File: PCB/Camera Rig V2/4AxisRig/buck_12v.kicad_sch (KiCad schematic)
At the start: 9 parts, among them U2 AN_SY8105

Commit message: PCB V2 first draft
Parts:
- C14, C15, C16: footprint (none) -> Capacitor_SMD:C_0603_1608Metric_Pad1.08x0.95mm_HandSolder
- C17, C18: footprint (none) -> Capacitor_SMD:C_1206_3216Metric_Pad1.33x1.80mm_HandSolder
- L1: footprint footprints:DR74 -> DR74-4R7-R:DR74; Unique FP y -> (none)
- U2: Unique FP y -> (none)
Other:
- moved on the sheet: C15
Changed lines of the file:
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@@
 	(wire
 		(pts
-			(xy 134.62 74.93) (xy 137.16 74.93)
+			(xy 133.35 74.93) (xy 137.16 74.93)
 		)
 		(stroke
@@
 	(wire
 		(pts
-			(xy 127 74.93) (xy 123.19 74.93)
+			(xy 125.73 74.93) (xy 123.19 74.93)
 		)
 		(stroke
@@
 			)
 		)
-		(property "Unique FP" ""
-			(at 147.32 105.41 0)
-			(effects
-				(font
-					(size 1.27 1.27)
-				)
-			)
-		)
 		(pin "2"
 		)
@@
 			)
 		)
-		(property "Footprint" ""
+		(property "Footprint" "Capacitor_SMD:C_0603_1608Metric_Pad1.08x0.95mm_HandSolder"
 			(at 94.9452 97.79 0)
 			(effects
@@
 		)
 		(property "Part Number" ""
-			(at 93.98 93.98 0)
-			(effects
-				(font
-					(size 1.27 1.27)
-				)
-			)
-		)
-		(property "Unique FP" ""
 			(at 93.98 93.98 0)
 			(effects
@@
 		(fields_autoplaced yes)
 		(property "Reference" "U2"
-			(at 125.3333 81.28 0)
+			(at 125.3333 80.01 0)
 			(effects
 				(font
@@
 		)
 		(property "Value" "AN_SY8105"
-			(at 125.3333 83.82 0)
+			(at 125.3333 82.55 0)
 			(effects
 				(font
@@
 					(size 1.27 1.27)
 				)
-			)
-		)
-		(property "Unique FP" "y"
-			(at 123.19 92.71 0)
-			(effects
-				(font
-					(size 1.27 1.27)
-				)
+				(hide yes)
 			)
 		)
@@
 			)
 		)
-		(property "Footprint" ""
+		(property "Footprint" "Capacitor_SMD:C_1206_3216Metric_Pad1.33x1.80mm_HandSolder"
 			(at 190.1952 99.06 0)
 			(effects
@@
 			)
 		)
-		(property "Datasheet" "~"
+		(property "Datasheet" "https://mm.digikey.com/Volume0/opasdata/d220001/medias/docus/506/TMK316BBJ226ML-T_SS.pdf"
 			(at 189.23 95.25 0)
 			(effects
@@
 		)
 		(property "Part Number" ""
-			(at 189.23 95.25 0)
-			(effects
-				(font
-					(size 1.27 1.27)
-				)
-			)
-		)
-		(property "Unique FP" ""
 			(at 189.23 95.25 0)
 			(effects
@@
 	(symbol
 		(lib_id "Device:C")
-		(at 130.81 74.93 270)
+		(at 129.54 74.93 270)
 		(unit 1)
 		(exclude_from_sim no)
@@
 		(fields_autoplaced yes)
 		(property "Reference" "C15"
-			(at 130.81 67.31 90)
+			(at 129.54 67.31 90)
 			(effects
 				(font
@@
 		)
 		(property "Value" "100nF"
-			(at 130.81 69.85 90)
-			(effects
-				(font
-					(size 1.27 1.27)
-				)
-			)
-		)
-		(property "Footprint" ""
-			(at 127 75.8952 0)
+			(at 129.54 69.85 90)
+			(effects
+				(font
+					(size 1.27 1.27)
+				)
+			)
+		)
+		(property "Footprint" "Capacitor_SMD:C_0603_1608Metric_Pad1.08x0.95mm_HandSolder"
+			(at 125.73 75.8952 0)
 			(effects
 				(font
@@
 		)
 		(property "Datasheet" "~"
-			(at 130.81 74.93 0)
+			(at 129.54 74.93 0)
 			(effects
 				(font
@@
 		)
 		(property "Description" "Unpolarized capacitor"
-			(at 130.81 74.93 0)
+			(at 129.54 74.93 0)
 			(effects
 				(font
@@
 		)
 		(property "Link" ""
-			(at 130.81 74.93 0)
+			(at 129.54 74.93 0)
 			(effects
 				(font
@@
 		)
 		(property "Part Number" ""
-			(at 130.81 74.93 0)
-			(effects
-				(font
-					(size 1.27 1.27)
-				)
-			)
-		)
-		(property "Unique FP" ""
-			(at 130.81 74.93 0)
+			(at 129.54 74.93 0)
 			(effects
 				(font
@@
 			)
 		)
-		(property "Footprint" "footprints:DR74"
+		(property "Footprint" "DR74-4R7-R:DR74"
 			(at 142.24 90.17 0)
 			(effects
@@
 					(size 1.27 1.27)
 				)
-			)
-		)
-		(property "Unique FP" "y"
-			(at 142.24 90.17 0)
-			(effects
-				(font
-					(size 1.27 1.27)
-				)
+				(hide yes)
 			)
 		)
@@
 			)
 		)
-		(property "Footprint" ""
+		(property "Footprint" "Capacitor_SMD:C_1206_3216Metric_Pad1.33x1.80mm_HandSolder"
 			(at 178.7652 99.06 0)
 			(effects
@@
 			)
 		)
-		(property "Datasheet" "~"
+		(property "Datasheet" "https://mm.digikey.com/Volume0/opasdata/d220001/medias/docus/506/TMK316BBJ226ML-T_SS.pdf"
 			(at 177.8 95.25 0)
 			(effects
@@
 		)
 		(property "Part Number" ""
-			(at 177.8 95.25 0)
-			(effects
-				(font
-					(size 1.27 1.27)
-				)
-			)
-		)
-		(property "Unique FP" ""
 			(at 177.8 95.25 0)
 			(effects
@@
 		(dnp no)
 		(property "Reference" "R15"
-			(at 142.748 97.282 90)
+			(at 149.606 94.234 0)
 			(effects
 				(font
@@
 		)
 		(property "Value" "200k"
-			(at 145.034 97.282 90)
+			(at 149.606 96.774 0)
 			(effects
 				(font
@@
 		)
 		(property "Part Number" ""
-			(at 147.32 95.25 0)
-			(effects
-				(font
-					(size 1.27 1.27)
-				)
-			)
-		)
-		(property "Unique FP" ""
 			(at 147.32 95.25 0)
 			(effects
@@
 			)
 		)
-		(property "Footprint" ""
+		(property "Footprint" "Capacitor_SMD:C_0603_1608Metric_Pad1.08x0.95mm_HandSolder"
 			(at 160.9852 99.06 0)
 			(effects
@@
 			(at 160.02 95.25 0)
 			(effects
-				(font
-					(size 1.27 1.27)
-				)
-			)
-		)
-		(property "Unique FP" ""
-			(at 160.02 95.25 0)
-			(effects

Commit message: Updated figs
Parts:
- added D6: SMAJ10CA-13-F, SMAJ10CA-13-F:SMA_DIO, symbol Device:D_Schottky
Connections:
- net GND: now also D6.1 (K)
- net VOUT_12V: now also D6.2 (A)
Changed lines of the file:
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@@
+	)
+	(junction
+		(at 203.2 90.17)
+		(diameter 0)
+		(color 0 0 0 0)
 	)
 	(junction
@@
 	(wire
 		(pts
+			(xy 203.2 91.44) (xy 203.2 90.17)
+		)
+		(stroke
+			(width 0)
+			(type default)
+		)
+	)
+	(wire
+		(pts
 			(xy 137.16 90.17) (xy 138.43 90.17)
 		)
@@
 	(wire
 		(pts
+			(xy 203.2 90.17) (xy 208.28 90.17)
+		)
+		(stroke
+			(width 0)
+			(type default)
+		)
+	)
+	(wire
+		(pts
 			(xy 147.32 100.33) (xy 147.32 99.06)
 		)
@@
 	(wire
 		(pts
-			(xy 189.23 90.17) (xy 194.31 90.17)
+			(xy 189.23 90.17) (xy 203.2 90.17)
 		)
 		(stroke
@@
 	(hierarchical_label "VOUT_12V"
 		(shape output)
-		(at 194.31 90.17 0)
+		(at 208.28 90.17 0)
 		(effects
 			(font
@@
 			)
 			(justify right)
+		)
+	)
+	(symbol
+		(lib_id "Device:D_Schottky")
+		(at 203.2 95.25 90)
+		(unit 1)
+		(exclude_from_sim no)
+		(in_bom yes)
+		(on_board yes)
+		(dnp no)
+		(fields_autoplaced yes)
+		(property "Reference" "D6"
+			(at 205.74 94.2974 90)
+			(effects
+				(font
+					(size 1.27 1.27)
+				)
+				(justify right)
+			)
+		)
+		(property "Value" "SMAJ10CA-13-F"
+			(at 205.74 96.8374 90)
+			(effects
+				(font
+					(size 1.27 1.27)
+				)
+				(justify right)
+			)
+		)
+		(property "Footprint" "SMAJ10CA-13-F:SMA_DIO"
+			(at 203.2 95.25 0)
+			(effects
+				(font
+					(size 1.27 1.27)
+				)
+				(hide yes)
+			)
+		)
+		(property "Datasheet" "https://www.diodes.com/assets/Datasheets/SMAJ5.0CA-SMAJ200CA.pdf"
+			(at 203.2 95.25 0)
+			(effects
+				(font
+					(size 1.27 1.27)
+				)
+				(hide yes)
+			)
+		)
+		(property "Description" "Schottky diode"
+			(at 203.2 95.25 0)
+			(effects
+				(font
+					(size 1.27 1.27)
+				)
+				(hide yes)
+			)
+		)
+		(property "Link" ""
+			(at 203.2 95.25 0)
+			(effects
+				(font
+					(size 1.27 1.27)
+				)
+			)
+		)
+		(property "Part Number" ""
+			(at 203.2 95.25 0)
+			(effects
+				(font
+					(size 1.27 1.27)
+				)
+			)
+		)
+		(pin "2"
+		)
+		(pin "1"
+		)
+		(instances
+			(project "4AxisRig"
+				(path "/afe116b2-64d1-4090-9b3d-2b16ecf9512b/ea896716-9127-4765-8811-1397e4644c8c"
+					(reference "D6")
+					(unit 1)
+				)
+			)
 		)
 	)
@@
 					(unit 1)
 				)
+			)
+		)
+	)
+	(symbol
+		(lib_id "power:GND")
+		(at 203.2 99.06 0)
+		(unit 1)
+		(exclude_from_sim no)
+		(in_bom yes)
+		(on_board yes)
+		(dnp no)
+		(fields_autoplaced yes)
+		(property "Reference" "#PWR0101"
+			(at 203.2 105.41 0)
+			(effects
+				(font
+					(size 1.27 1.27)
+				)
+				(hide yes)
+			)
+		)
+		(property "Value" "GND"
+			(at 203.2 104.14 0)
+			(effects
+				(font
+					(size 1.27 1.27)
+				)
+			)
+		)
+		(property "Footprint" ""
+			(at 203.2 99.06 0)
+			(effects
+				(font
+					(size 1.27 1.27)
+				)
+				(hide yes)
+			)
+		)
+		(property "Datasheet" ""
+			(at 203.2 99.06 0)
+			(effects
+				(font
+					(size 1.27 1.27)
+				)
+				(hide yes)
+			)
+		)
+		(property "Description" "Power symbol creates a global label with name \"GND\" , ground"
+			(at 203.2 99.06 0)
+			(effects
+				(font
+					(size 1.27 1.27)
+				)
+				(hide yes)
+			)
+		)
+		(pin "1"
+		)
+		(instances
+			(project "4AxisRig"
+				(path "/afe116b2-64d1-4090-9b3d-2b16ecf9512b/ea896716-9127-4765-8811-1397e4644c8c"
+					(reference "#PWR0101")
+					(unit 1)
+				)

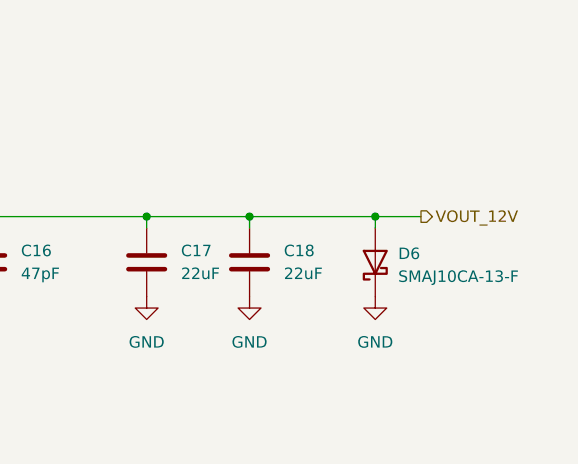
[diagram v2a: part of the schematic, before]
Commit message: Netclass Improvements
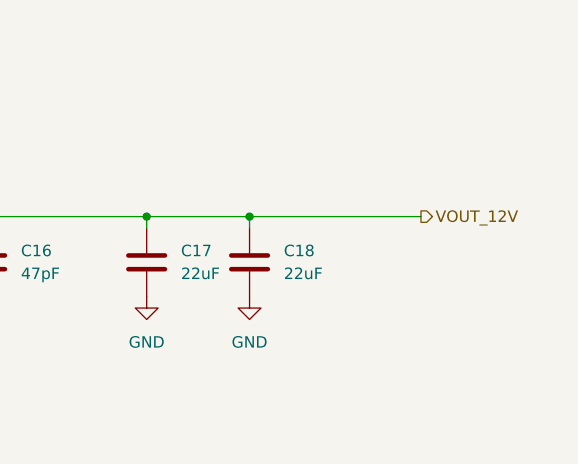
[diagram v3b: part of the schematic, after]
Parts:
- removed D6: SMAJ10CA-13-F, SMAJ10CA-13-F:SMA_DIO, symbol Device:D_Schottky
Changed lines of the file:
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@@
-	)
-	(junction
-		(at 203.2 90.17)
-		(diameter 0)
-		(color 0 0 0 0)
 	)
 	(junction
@@
 	(wire
 		(pts
-			(xy 203.2 91.44) (xy 203.2 90.17)
-		)
-		(stroke
-			(width 0)
-			(type default)
-		)
-	)
-	(wire
-		(pts
 			(xy 137.16 90.17) (xy 138.43 90.17)
 		)
@@
 	(wire
 		(pts
-			(xy 203.2 90.17) (xy 208.28 90.17)
-		)
-		(stroke
-			(width 0)
-			(type default)
-		)
-	)
-	(wire
-		(pts
 			(xy 147.32 100.33) (xy 147.32 99.06)
 		)
@@
 	(wire
 		(pts
-			(xy 189.23 90.17) (xy 203.2 90.17)
+			(xy 189.23 90.17) (xy 208.28 90.17)
 		)
 		(stroke
@@
 		)
 	)
-	(symbol
-		(lib_id "Device:D_Schottky")
-		(at 203.2 95.25 90)
-		(unit 1)
-		(exclude_from_sim no)
-		(in_bom yes)
-		(on_board yes)
-		(dnp no)
+	(netclass_flag ""
+		(length 2.54)
+		(shape round)
+		(at 160.02 100.33 180)
 		(fields_autoplaced yes)
-		(property "Reference" "D6"
-			(at 205.74 94.2974 90)
-			(effects
-				(font
-					(size 1.27 1.27)
-				)
-				(justify right)
-			)
-		)
-		(property "Value" "SMAJ10CA-13-F"
-			(at 205.74 96.8374 90)
-			(effects
-				(font
-					(size 1.27 1.27)
-				)
-				(justify right)
-			)
-		)
-		(property "Footprint" "SMAJ10CA-13-F:SMA_DIO"
-			(at 203.2 95.25 0)
-			(effects
-				(font
-					(size 1.27 1.27)
-				)
-				(hide yes)
-			)
-		)
-		(property "Datasheet" "https://www.diodes.com/assets/Datasheets/SMAJ5.0CA-SMAJ200CA.pdf"
-			(at 203.2 95.25 0)
-			(effects
-				(font
-					(size 1.27 1.27)
-				)
-				(hide yes)
-			)
-		)
-		(property "Description" "Schottky diode"
-			(at 203.2 95.25 0)
-			(effects
-				(font
-					(size 1.27 1.27)
-				)
-				(hide yes)
-			)
-		)
-		(property "Link" ""
-			(at 203.2 95.25 0)
-			(effects
-				(font
-					(size 1.27 1.27)
-				)
-			)
-		)
-		(property "Part Number" ""
-			(at 203.2 95.25 0)
-			(effects
-				(font
-					(size 1.27 1.27)
-				)
-			)
-		)
-		(pin "2"
-		)
-		(pin "1"
-		)
-		(instances
-			(project "4AxisRig"
-				(path "/afe116b2-64d1-4090-9b3d-2b16ecf9512b/ea896716-9127-4765-8811-1397e4644c8c"
-					(reference "D6")
-					(unit 1)
+		(effects
+			(font
+				(size 1.27 1.27)
+			)
+			(justify right bottom)
+		)
+		(property "Netclass" "Power SW (~100kHz)"
+			(at 160.7185 102.87 0)
+			(effects
+				(font
+					(size 1.27 1.27)
+				)
+				(justify left)
+			)
+		)
+		(property "Component Class" ""
+			(at -207.01 11.43 0)
+			(effects
+				(font
+					(size 1.27 1.27)
+					(italic yes)
+				)
+			)
+		)
+	)
+	(netclass_flag ""
+		(length 2.54)
+		(shape round)
+		(at 137.16 74.93 270)
+		(effects
+			(font
+				(size 1.27 1.27)
+			)
+			(justify right bottom)
+		)
+		(property "Netclass" "Power SW (~100kHz)"
+			(at 140.97 74.676 0)
+			(effects
+				(font
+					(size 1.27 1.27)
+				)
+				(justify left)
+			)
+		)
+		(property "Component Class" ""
+			(at -229.87 -13.97 0)
+			(effects
+				(font
+					(size 1.27 1.27)
+					(italic yes)
+				)
+			)
+		)
+	)
+	(netclass_flag ""
+		(length 2.54)
+		(shape round)
+		(at 123.19 74.93 90)
+		(effects
+			(font
+				(size 1.27 1.27)
+			)
+			(justify left bottom)
+		)
+		(property "Netclass" "Power SW (~100kHz)"
+			(at 97.79 74.676 0)
+			(effects
+				(font
+					(size 1.27 1.27)
+				)
+				(justify left)
+			)
+		)
+		(property "Component Class" ""
+			(at -243.84 -13.97 0)
+			(effects
+				(font
+					(size 1.27 1.27)
+					(italic yes)
 				)
 			)
@@
 					(unit 1)
 				)
-			)
-		)
-	)
-	(symbol
-		(lib_id "power:GND")
-		(at 203.2 99.06 0)
-		(unit 1)
-		(exclude_from_sim no)
-		(in_bom yes)
-		(on_board yes)
-		(dnp no)
-		(fields_autoplaced yes)
-		(property "Reference" "#PWR0101"
-			(at 203.2 105.41 0)
-			(effects
-				(font
-					(size 1.27 1.27)
-				)
-				(hide yes)
-			)
-		)
-		(property "Value" "GND"
-			(at 203.2 104.14 0)
-			(effects
-				(font
-					(size 1.27 1.27)
-				)
-			)
-		)
-		(property "Footprint" ""
-			(at 203.2 99.06 0)
-			(effects
-				(font
-					(size 1.27 1.27)
-				)
-				(hide yes)
-			)
-		)
-		(property "Datasheet" ""
-			(at 203.2 99.06 0)
-			(effects
-				(font
-					(size 1.27 1.27)
-				)
-				(hide yes)
-			)
-		)
-		(property "Description" "Power symbol creates a global label with name \"GND\" , ground"
-			(at 203.2 99.06 0)
-			(effects
-				(font
-					(size 1.27 1.27)
-				)
-				(hide yes)
-			)
-		)
-		(pin "1"
-		)
-		(instances
-			(project "4AxisRig"
-				(path "/afe116b2-64d1-4090-9b3d-2b16ecf9512b/ea896716-9127-4765-8811-1397e4644c8c"
-					(reference "#PWR0101")
-					(unit 1)
-				)
